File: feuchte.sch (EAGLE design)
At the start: 17 parts, among them IC1 ULN2003AD, IC2 IP4234CZ6, K1 G5LA, Q1 12MHz, U1 ATMEGA32U2-AU

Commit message: Bibliothek hinzugefügt
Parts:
- C1, C4, C5, C6, C7: device eigene:C -> Bauelemente:C
- C2, C3: device resistor:C-EUC0603K -> Bauelemente:C
- IC2: value IP4234CZ6 -> ESD_USB_IP4234CZ6; device eigene:IP4234CZ6 -> Bauelemente:ESD_USB_IP4234CZ6
- K1: value G5LA -> RELAY_G5LA; device eigene:G5LA -> Bauelemente:RELAY_G5LA
- Q1: device eigene:QUARZ-ABMM2 -> Bauelemente:QUARTZ_ABMM2
- R1, R2, R3: device eigene:R -> Bauelemente:R
- U$1: value CON-SPI-10 -> CON_SPI_AVR10; device eigene:CON-SPI-10 -> Bauelemente:CON_SPI_AVR10
- U1: value ATMEGA32U2-AU -> MCU_ATMEGA32U2-AU; device eigene:ATMEGA32U2-AU -> Bauelemente:MCU_ATMEGA32U2-AU
- USB1: value CON-MICROUSB-ZX62R-B-5P -> CON_MICROUSB_ZX62R-B-5P; device eigene:CON-MICROUSB-ZX62R-B-5P -> Bauelemente:CON_MICROUSB_ZX62R-B-5P
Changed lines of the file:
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@@
 </classes>
 <parts>
-<part name="U1" library="eigene" deviceset="ATMEGA32U2-AU" device=""/>
-<part name="K1" library="eigene" deviceset="G5LA" device=""/>
+<part name="U1" library="Bauelemente" deviceset="MCU_ATMEGA32U2-AU" device=""/>
+<part name="K1" library="Bauelemente" deviceset="RELAY_G5LA" device=""/>
 <part name="IC1" library="uln-udn" deviceset="ULN2003A" device="D"/>
-<part name="R1" library="eigene" deviceset="R" device="" value="1k"/>
-<part name="C1" library="eigene" deviceset="C" device="" value="100n"/>
-<part name="Q1" library="eigene" deviceset="QUARZ-ABMM2" device="" value="12MHz"/>
-<part name="C2" library="resistor" deviceset="C-EU" device="C0603K" value="33p"/>
-<part name="C3" library="resistor" deviceset="C-EU" device="C0603K" value="33p"/>
-<part name="C4" library="eigene" deviceset="C" device="" value="100n"/>
-<part name="C5" library="eigene" deviceset="C" device="" value="1µ"/>
-<part name="C6" library="eigene" deviceset="C" device="" value="10µ"/>
-<part name="R2" library="eigene" deviceset="R" device="" value="22"/>
-<part name="R3" library="eigene" deviceset="R" device="" value="22"/>
-<part name="USB1" library="eigene" deviceset="CON-MICROUSB-ZX62R-B-5P" device=""/>
-<part name="IC2" library="eigene" deviceset="IP4234CZ6" device=""/>
+<part name="R1" library="Bauelemente" deviceset="R" device="" value="1k"/>
+<part name="C1" library="Bauelemente" deviceset="C" device="" value="100n"/>
+<part name="Q1" library="Bauelemente" deviceset="QUARTZ_ABMM2" device="" value="12MHz"/>
+<part name="C2" library="Bauelemente" deviceset="C" device="" value="33p"/>
+<part name="C3" library="Bauelemente" deviceset="C" device="" value="33p"/>
+<part name="C4" library="Bauelemente" deviceset="C" device="" value="100n"/>
+<part name="C5" library="Bauelemente" deviceset="C" device="" value="1µ"/>
+<part name="C6" library="Bauelemente" deviceset="C" device="" value="10µ"/>
+<part name="R2" library="Bauelemente" deviceset="R" device="" value="22"/>
+<part name="R3" library="Bauelemente" deviceset="R" device="" value="22"/>
+<part name="USB1" library="Bauelemente" deviceset="CON_MICROUSB_ZX62R-B-5P" device=""/>
+<part name="IC2" library="Bauelemente" deviceset="ESD_USB_IP4234CZ6" device=""/>
 <part name="P+1" library="supply1" deviceset="+5V" device=""/>
 <part name="GND1" library="supply1" deviceset="GND" device=""/>
@@
 <part name="GND5" library="supply1" deviceset="GND" device=""/>
 <part name="GND6" library="supply1" deviceset="GND" device=""/>
-<part name="U$1" library="eigene" deviceset="CON-SPI-10" device=""/>
+<part name="U$1" library="Bauelemente" deviceset="CON_SPI_AVR10" device=""/>
 <part name="P+3" library="supply1" deviceset="+5V" device=""/>
 <part name="GND7" library="supply1" deviceset="GND" device=""/>
-<part name="C7" library="eigene" deviceset="C" device="" value="100n"/>
+<part name="C7" library="Bauelemente" deviceset="C" device="" value="100n"/>
 </parts>
 <sheets>

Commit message: SMD Bauteile auf Rückseite gespiegelt
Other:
- moved on the sheet: C7, R1
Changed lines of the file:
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@@
 <?xml version="1.0" encoding="utf-8"?>
 <!DOCTYPE eagle SYSTEM "eagle.dtd">
-<eagle version="6.5.0">
+<eagle version="6.6.0">
 <drawing>
 <settings>
@@
 <instance part="K1" gate="G$2" x="187.96" y="76.2"/>
 <instance part="IC1" gate="A" x="170.18" y="58.42"/>
-<instance part="R1" gate="G$1" x="134.62" y="27.94"/>
+<instance part="R1" gate="G$1" x="137.16" y="35.56"/>
 <instance part="C1" gate="G$1" x="17.78" y="63.5" rot="R180"/>
 <instance part="Q1" gate="G$1" x="45.72" y="40.64" rot="R270"/>
@@
 <instance part="P+3" gate="1" x="121.92" y="78.74"/>
 <instance part="GND7" gate="1" x="121.92" y="60.96"/>
-<instance part="C7" gate="G$1" x="152.4" y="27.94"/>
+<instance part="C7" gate="G$1" x="124.46" y="33.02"/>
 </instances>
 <busses>

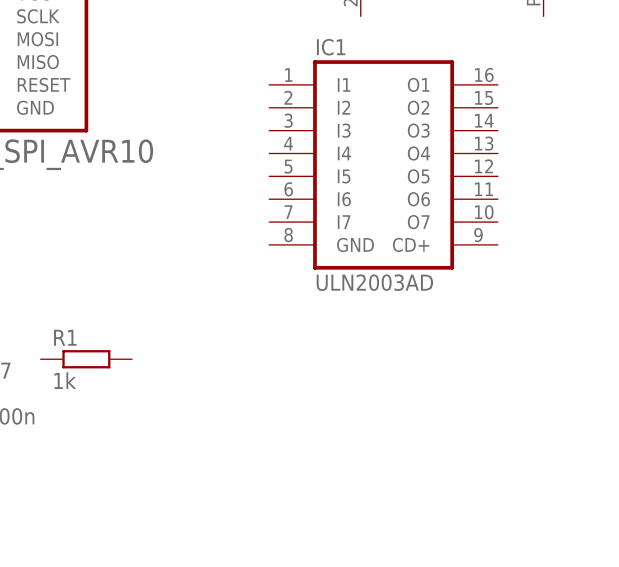
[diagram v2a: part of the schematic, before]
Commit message: ULN2003 aus Eagle verändert um fehler vom DRC zu entfernen und besser dem Datenblatt zu entsprechen
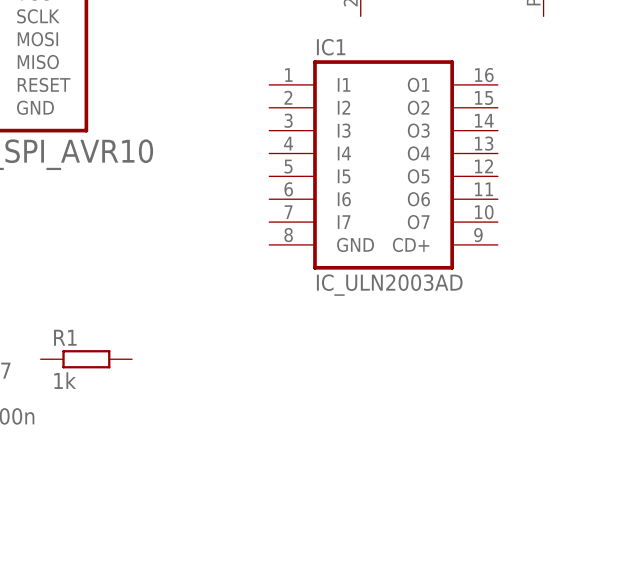
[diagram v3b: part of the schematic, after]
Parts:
- IC1: value ULN2003AD -> IC_ULN2003AD; device uln-udn:ULN2003AD -> Bauelemente:IC_ULN2003AD
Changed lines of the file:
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@@
 <part name="U1" library="Bauelemente" deviceset="MCU_ATMEGA32U2-AU" device=""/>
 <part name="K1" library="Bauelemente" deviceset="RELAY_G5LA" device=""/>
-<part name="IC1" library="uln-udn" deviceset="ULN2003A" device="D"/>
+<part name="IC1" library="Bauelemente" deviceset="IC_ULN2003A" device="D"/>
 <part name="R1" library="Bauelemente" deviceset="R" device="" value="1k"/>
 <part name="C1" library="Bauelemente" deviceset="C" device="" value="100n"/>

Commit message: abends gehts nach hause
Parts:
- added C10, C8, C9: 100n, Bauelemente:C
- added CON1, CON2: CON_PCB_7.5MM_3-POLE, Bauelemente:CON_PCB_7.5MM_3-POLE
- added K2: RELAY_G5LA, Bauelemente:RELAY_G5LA
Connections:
- new net +3V3: C5.2, U1.+3V3
- new net CAP: R1.2
- new net N$10: C10.1, C9.2
- new net N$11: IC1.I2, U1.(OC1A)_PC6
- new net N$13: IC1.O7, K1G$1.1
- new net N$14: IC1.O2, K2G$1.2
- new net N$15: CON1.1, K1G$2.S
- new net N$16: CON1.3, K1G$2.O
- new net N$17: CON2.1, K2G$2.S
- new net N$18: CON2.2, K2G$2.P
- new net N$19: CON2.3, K2G$2.O
- new net N$7: CON1.2, K1G$2.P
- new net N$8: C7.1, C8.1, C9.1, U1.(AIN0)_PD1
- new net N$9: C10.2, C7.2, C8.2, R1.1, U1.(RXD1/AIN1)_PD2
- net +5V: now also IC1.CD+, K1G$1.2, K2G$1.1
- net GND: now also IC1.GND, Q1.GND; no longer Q1.GROUND
- net N$12: now also IC1.I7, U1.(OC0A/OC1C)_PB7; no longer C5.2, U1.UCAP_(+3V3)
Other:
- moved on the sheet: K1, R1
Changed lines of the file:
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@@
 <part name="GND7" library="supply1" deviceset="GND" device=""/>
 <part name="C7" library="Bauelemente" deviceset="C" device="" value="100n"/>
+<part name="C8" library="Bauelemente" deviceset="C" device="" value="100n"/>
+<part name="C9" library="Bauelemente" deviceset="C" device="" value="100n"/>
+<part name="C10" library="Bauelemente" deviceset="C" device="" value="100n"/>
+<part name="P+4" library="supply1" deviceset="+5V" device=""/>
+<part name="GND8" library="supply1" deviceset="GND" device=""/>
+<part name="P+5" library="supply1" deviceset="+5V" device=""/>
+<part name="K2" library="Bauelemente" deviceset="RELAY_G5LA" device=""/>
+<part name="P+6" library="supply1" deviceset="+5V" device=""/>
+<part name="CON1" library="Bauelemente" deviceset="CON_PCB_7.5MM_3-POLE" device=""/>
+<part name="CON2" library="Bauelemente" deviceset="CON_PCB_7.5MM_3-POLE" device=""/>
 </parts>
 <sheets>
@@
 <instances>
 <instance part="U1" gate="A" x="78.74" y="48.26"/>
-<instance part="K1" gate="G$1" x="167.64" y="78.74"/>
+<instance part="K1" gate="G$1" x="167.64" y="78.74" rot="R180"/>
 <instance part="K1" gate="G$2" x="187.96" y="76.2"/>
 <instance part="IC1" gate="A" x="170.18" y="58.42"/>
-<instance part="R1" gate="G$1" x="137.16" y="35.56"/>
+<instance part="R1" gate="G$1" x="170.18" y="27.94"/>
 <instance part="C1" gate="G$1" x="17.78" y="63.5" rot="R180"/>
 <instance part="Q1" gate="G$1" x="45.72" y="40.64" rot="R270"/>
@@
 <instance part="GND7" gate="1" x="121.92" y="60.96"/>
 <instance part="C7" gate="G$1" x="124.46" y="33.02"/>
+<instance part="C8" gate="G$1" x="134.62" y="33.02"/>
+<instance part="C9" gate="G$1" x="139.7" y="35.56" rot="R90"/>
+<instance part="C10" gate="G$1" x="144.78" y="33.02"/>
+<instance part="P+4" gate="1" x="167.64" y="86.36"/>
+<instance part="GND8" gate="1" x="157.48" y="45.72"/>
+<instance part="P+5" gate="1" x="190.5" y="50.8"/>
+<instance part="K2" gate="G$1" x="203.2" y="78.74"/>
+<instance part="K2" gate="G$2" x="231.14" y="73.66"/>
+<instance part="P+6" gate="1" x="203.2" y="86.36"/>
+<instance part="CON1" gate="A" x="187.96" y="101.6" rot="MR270"/>
+<instance part="CON2" gate="A" x="231.14" y="101.6" rot="MR270"/>
 </instances>
 <busses>
@@
 <pinref part="GND3" gate="1" pin="GND"/>
 <junction x="38.1" y="38.1"/>
-<pinref part="Q1" gate="G$1" pin="GROUND"/>
+<pinref part="Q1" gate="G$1" pin="GND"/>
 <wire x1="38.1" y1="40.64" x2="38.1" y2="38.1" width="0.1524" layer="91"/>
 <wire x1="40.64" y1="40.64" x2="38.1" y2="40.64" width="0.1524" layer="91"/>
@@
 <pinref part="U$1" gate="1" pin="GND"/>
 <pinref part="GND7" gate="1" pin="GND"/>
+</segment>
+<segment>
+<pinref part="IC1" gate="A" pin="GND"/>
+<pinref part="GND8" gate="1" pin="GND"/>
 </segment>
 </net>
@@
 <pinref part="P+3" gate="1" pin="+5V"/>
 </segment>
+<segment>
+<pinref part="K1" gate="G$1" pin="2"/>
+<pinref part="P+4" gate="1" pin="+5V"/>
+</segment>
+<segment>
+<pinref part="P+5" gate="1" pin="+5V"/>
+<pinref part="IC1" gate="A" pin="CD+"/>
+<wire x1="190.5" y1="48.26" x2="182.88" y2="48.26" width="0.1524" layer="91"/>
+</segment>
+<segment>
+<pinref part="K2" gate="G$1" pin="1"/>
+<pinref part="P+6" gate="1" pin="+5V"/>
+</segment>
 </net>
 <net name="USBR_P" class="0">
@@
 </segment>
 </net>
-<net name="N$12" class="0">
-<segment>
-<pinref part="U1" gate="A" pin="UCAP_(+3V3)"/>
+<net name="+3V3" class="0">
+<segment>
+<pinref part="U1" gate="A" pin="+3V3"/>
 <pinref part="C5" gate="G$1" pin="2"/>
 </segment>
@@
 </segment>
 </net>
+<net name="N$8" class="0">
+<segment>
+<pinref part="U1" gate="A" pin="(AIN0)_PD1"/>
+<pinref part="C7" gate="G$1" pin="1"/>
+<wire x1="106.68" y1="35.56" x2="124.46" y2="35.56" width="0.1524" layer="91"/>
+<pinref part="C9" gate="G$1" pin="1"/>
+<pinref part="C8" gate="G$1" pin="1"/>
+<wire x1="137.16" y1="35.56" x2="134.62" y2="35.56" width="0.1524" layer="91"/>
+<wire x1="124.46" y1="35.56" x2="134.62" y2="35.56" width="0.1524" layer="91"/>
+<junction x="124.46" y="35.56"/>
+<junction x="134.62" y="35.56"/>
+</segment>
+</net>
+<net name="N$9" class="0">
+<segment>
+<pinref part="U1" gate="A" pin="(RXD1/AIN1)_PD2"/>
+<wire x1="106.68" y1="33.02" x2="114.3" y2="33.02" width="0.1524" layer="91"/>
+<wire x1="114.3" y1="33.02" x2="114.3" y2="27.94" width="0.1524" layer="91"/>
+<pinref part="C7" gate="G$1" pin="2"/>
+<wire x1="114.3" y1="27.94" x2="124.46" y2="27.94" width="0.1524" layer="91"/>
+<pinref part="R1" gate="G$1" pin="1"/>
+<wire x1="124.46" y1="27.94" x2="134.62" y2="27.94" width="0.1524" layer="91"/>
+<junction x="124.46" y="27.94"/>
+<pinref part="C8" gate="G$1" pin="2"/>
+<wire x1="134.62" y1="27.94" x2="144.78" y2="27.94" width="0.1524" layer="91"/>
+<junction x="134.62" y="27.94"/>
+<pinref part="C10" gate="G$1" pin="2"/>
+<wire x1="144.78" y1="27.94" x2="165.1" y2="27.94" width="0.1524" layer="91"/>
+<junction x="144.78" y="27.94"/>
+</segment>
+</net>
+<net name="CAP" class="0">
+<segment>
+<pinref part="R1" gate="G$1" pin="2"/>
+<wire x1="175.26" y1="27.94" x2="182.88" y2="27.94" width="0.1524" layer="91"/>
+</segment>
+</net>
+<net name="N$10" class="0">
+<segment>
+<pinref part="C9" gate="G$1" pin="2"/>
+<pinref part="C10" gate="G$1" pin="1"/>
+</segment>
+</net>
+<net name="N$11" class="0">
+<segment>
+<wire x1="147.32" y1="45.72" x2="147.32" y2="63.5" width="0.1524" layer="91"/>
+<pinref part="U1" gate="A" pin="(OC1A)_PC6"/>
+<wire x1="147.32" y1="45.72" x2="106.68" y2="45.72" width="0.1524" layer="91"/>
+<pinref part="IC1" gate="A" pin="I2"/>
+<wire x1="147.32" y1="63.5" x2="157.48" y2="63.5" width="0.1524" layer="91"/>
+</segment>
+</net>
+<net name="N$13" class="0">
+<segment>
+<wire x1="187.96" y1="50.8" x2="187.96" y2="71.12" width="0.1524" layer="91"/>
+<wire x1="187.96" y1="71.12" x2="167.64" y2="71.12" width="0.1524" layer="91"/>
+<pinref part="K1" gate="G$1" pin="1"/>
+<wire x1="167.64" y1="71.12" x2="167.64" y2="73.66" width="0.1524" layer="91"/>
+<pinref part="IC1" gate="A" pin="O7"/>
+<wire x1="182.88" y1="50.8" x2="187.96" y2="50.8" width="0.1524" layer="91"/>
+</segment>
+</net>
+<net name="N$12" class="0">
+<segment>
+<pinref part="U1" gate="A" pin="(OC0A/OC1C)_PB7"/>
+<wire x1="149.86" y1="55.88" x2="106.68" y2="55.88" width="0.1524" layer="91"/>
+<wire x1="106.68" y1="55.88" x2="106.68" y2="58.42" width="0.1524" layer="91"/>
+<pinref part="IC1" gate="A" pin="I7"/>
+<wire x1="157.48" y1="50.8" x2="149.86" y2="50.8" width="0.1524" layer="91"/>
+<wire x1="149.86" y1="50.8" x2="149.86" y2="55.88" width="0.1524" layer="91"/>
+</segment>
+</net>
+<net name="N$7" class="0">
+<segment>
+<pinref part="K1" gate="G$2" pin="P"/>
+<pinref part="CON1" gate="A" pin="2"/>
+<wire x1="187.96" y1="73.66" x2="187.96" y2="91.44" width="0.1524" layer="91"/>
+</segment>
+</net>
+<net name="N$15" class="0">
+<segment>
+<pinref part="K1" gate="G$2" pin="S"/>
+<pinref part="CON1" gate="A" pin="1"/>
+<wire x1="182.88" y1="81.28" x2="185.42" y2="81.28" width="0.1524" layer="91"/>
+<wire x1="185.42" y1="81.28" x2="185.42" y2="91.44" width="0.1524" layer="91"/>
+</segment>
+</net>
+<net name="N$16" class="0">
+<segment>
+<pinref part="K1" gate="G$2" pin="O"/>
+<pinref part="CON1" gate="A" pin="3"/>
+<wire x1="193.04" y1="81.28" x2="190.5" y2="81.28" width="0.1524" layer="91"/>
+<wire x1="190.5" y1="81.28" x2="190.5" y2="91.44" width="0.1524" layer="91"/>
+</segment>
+</net>
+<net name="N$17" class="0">
+<segment>
+<pinref part="K2" gate="G$2" pin="S"/>
+<pinref part="CON2" gate="A" pin="1"/>
+<wire x1="226.06" y1="78.74" x2="228.6" y2="78.74" width="0.1524" layer="91"/>
+<wire x1="228.6" y1="78.74" x2="228.6" y2="91.44" width="0.1524" layer="91"/>
+</segment>
+</net>
+<net name="N$18" class="0">
+<segment>
+<pinref part="K2" gate="G$2" pin="P"/>
+<pinref part="CON2" gate="A" pin="2"/>
+<wire x1="231.14" y1="71.12" x2="231.14" y2="91.44" width="0.1524" layer="91"/>
+</segment>
+</net>
+<net name="N$19" class="0">
+<segment>
+<pinref part="K2" gate="G$2" pin="O"/>
+<pinref part="CON2" gate="A" pin="3"/>
+<wire x1="236.22" y1="78.74" x2="233.68" y2="78.74" width="0.1524" layer="91"/>
+<wire x1="233.68" y1="78.74" x2="233.68" y2="91.44" width="0.1524" layer="91"/>
+</segment>
+</net>
+<net name="N$14" class="0">
+<segment>
+<pinref part="IC1" gate="A" pin="O2"/>
+<pinref part="K2" gate="G$1" pin="2"/>
+<wire x1="182.88" y1="63.5" x2="203.2" y2="63.5" width="0.1524" layer="91"/>
+<wire x1="203.2" y1="63.5" x2="203.2" y2="73.66" width="0.1524" layer="91"/>
+</segment>
+</net>
